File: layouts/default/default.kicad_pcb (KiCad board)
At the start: 2 copper layers, 66 parts

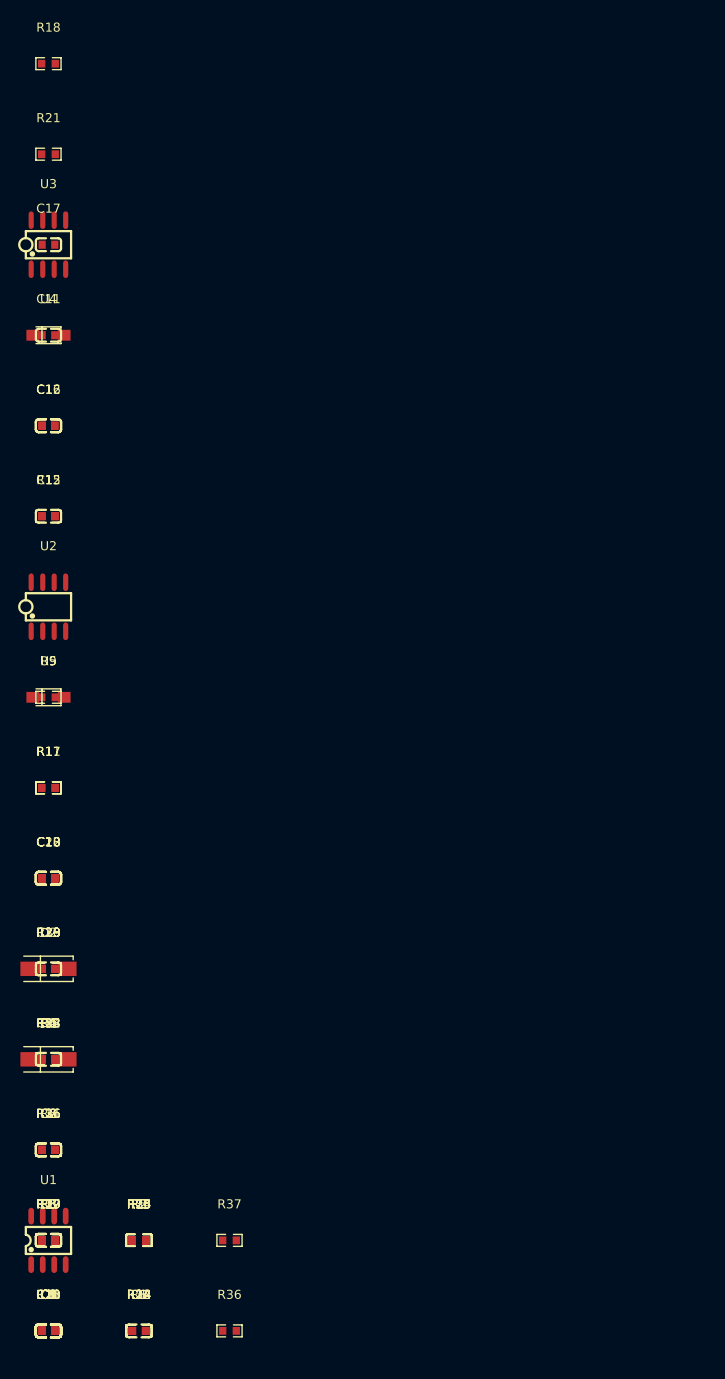
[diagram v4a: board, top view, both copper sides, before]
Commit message: Added plugin to show atopile_address on layout
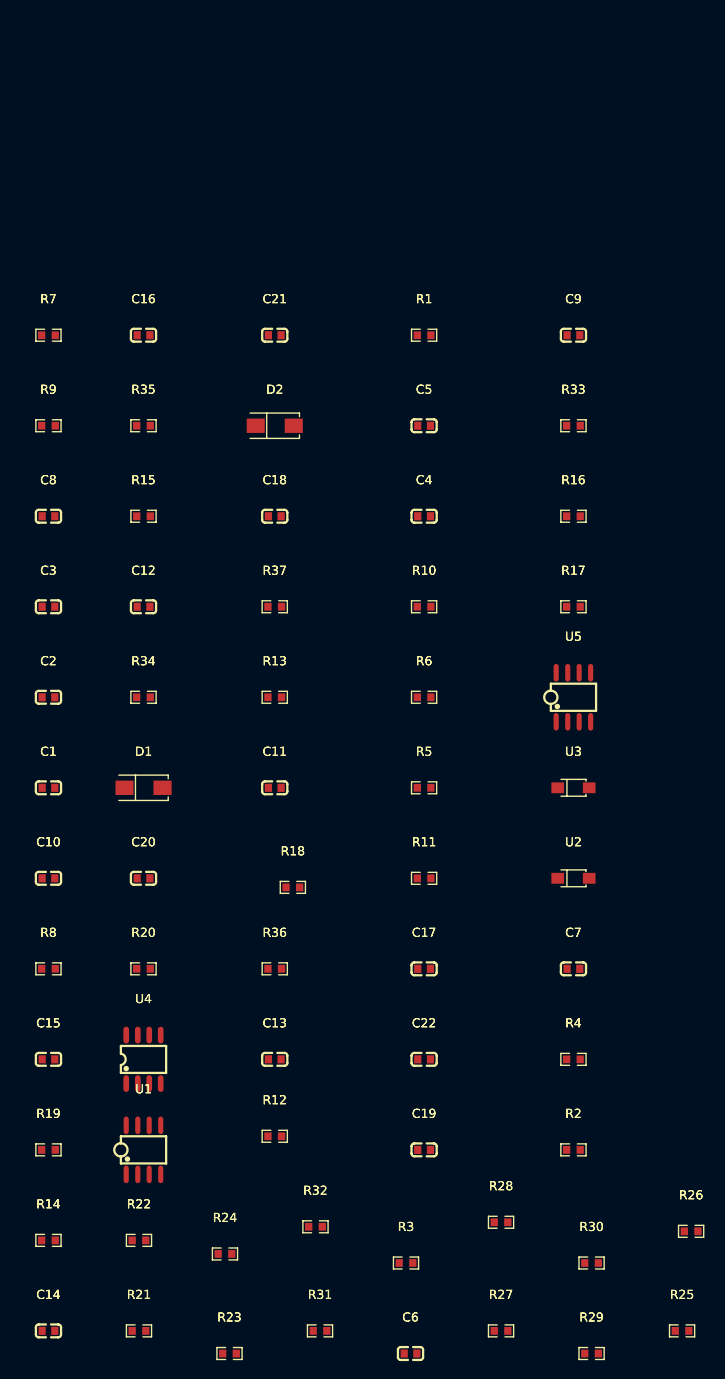
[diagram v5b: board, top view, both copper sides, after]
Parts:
- U1: footprint atopile:SOP-8_L4.9-W3.9-P1.27-LS6.0-BL-0d1ac6 -> atopile:SOIC-8_L5.0-W4.0-P1.27-LS6.0-BL-294f77
- U2, U3: footprint atopile:SOIC-8_L5.0-W4.0-P1.27-LS6.0-BL-294f77 -> atopile:SOD-123FL_L2.7-W1.8-LS3.8-RD-0c8348
- U4: footprint atopile:SOD-123FL_L2.7-W1.8-LS3.8-RD-0c8348 -> atopile:SOP-8_L4.9-W3.9-P1.27-LS6.0-BL-0d1ac6
- U5: footprint atopile:SOD-123FL_L2.7-W1.8-LS3.8-RD-0c8348 -> atopile:SOIC-8_L5.0-W4.0-P1.27-LS6.0-BL-294f77
- moved R21 130.4 mm to (10.0, 0.00)
- moved C9 124.4 mm to (58.0, -110.0)
- moved R1 114.4 mm to (41.5, -110.0)
- moved C21 112.8 mm to (25.0, -110.0)
- moved C4 99.1 mm to (41.5, -90.0)
- moved C5 99.1 mm to (41.5, -100.0)
- moved R18 94.9 mm to (27.0, -49.0)
- moved R16 90.9 mm to (58.0, -90.0)
- moved R15 90.6 mm to (10.5, -90.0)
- moved C8 90.6 mm to (0.00, -90.0)
- moved C17 90.1 mm to (41.5, -40.0)
- moved R10 90.1 mm to (41.5, -80.0)
- moved R35 90.0 mm to (10.5, -100.0)
- moved R7 90.0 mm to (0.00, -110.0)
- moved R33 83.5 mm to (58.0, -100.0)
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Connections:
- C1 pad 1: hv-1 -> net-2
- C1 pad 2: gnd-2 -> non_inverting_input
- C10 pad 1: INPUT-1 -> net-6
- C10 pad 2: resistors_ifs[0] -> P1INminus
- C11 pad 1: resistors_ifs[0] -> non_inverting_input
- C11 pad 2: net-6 -> line-1
- C12 pad 1: net-2 -> line-1
- C12 pad 2: net -> resistors_ifs[0]-2
- C13 pad 1: net-1 -> net-8
- C13 pad 2: P1INminus -> P2INminus-1
- C14 pad 1: line-1 -> P2INminus-1
- C14 pad 2: resistors_ifs[0]-1 -> P2OUT-1
- C15 pad 1: net-5 -> P2OUT-1
- C15 pad 2: P2INminus -> net
- C16 pad 1: P2INminus -> cathode
- C16 pad 2: P2OUT -> net-1
- C17 pad 1: P2OUT -> non_inverting_input
- C17 pad 2: net-7 -> gnd-2
- C18 pad 1: cathode -> P2OUT
- C18 pad 2: net -> net-7
- C19 pad 1: P1INminus -> VCCplus
- C19 pad 2: output -> gnd-2
- C2 pad 1: non_inverting_input -> hv-1
- C20 pad 1: wiper-1 -> gnd
- C20 pad 2: P2INminus-1 -> gnd-2
- C21 pad 1: non_inverting_input -> P1INminus
- C21 pad 2: net-4 -> output
- C22 pad 1: P2OUT-1 -> wiper
- C22 pad 2: net-8 -> P2INminus
- C3 pad 1: gnd -> CAPminus
- C3 pad 2: gnd-2 -> CAPplus
- C4 pad 1: CAPminus -> CAPplus
- C4 pad 2: CAPplus -> anode
- C5 pad 1: CAPplus -> non_inverting_input
- C5 pad 2: cathode-1 -> net-5
- C6 pad 1: VCCplus -> line
- C6 pad 2: gnd-2 -> ff1_low_pass-gnd
- C7 pad 1: net-3 -> INPUT
- C7 pad 2: non_inverting_input -> resistors_ifs[0]-3
- C8 pad 1: line -> resistors_ifs[0]-3
- C8 pad 2: ff1_low_pass-gnd -> net-4
- C9 pad 1: non_inverting_input -> net-3
- C9 pad 2: line-1 -> net-1
- D1 pad 1: cathode-1 -> anode
- D2 pad 2: cathode-1 -> anode
- R1 pad 1: non_inverting_input -> net-5
- R10 pad 1: wiper -> wiper-1
- R10 pad 2: net-2 -> net-6
- R11 pad 1: wiper -> line-1
- R11 pad 2: P1INminus -> resistors_ifs[0]-2
- R12 pad 1: wiper -> resistors_ifs[1]
- R12 pad 2: net-1 -> net-8
- R13 pad 1: resistors_ifs[0] -> net-8
- R13 pad 2: wiper -> P2INminus-1
- R14 pad 1: non_inverting_input -> P2INminus-1
- R14 pad 2: wiper -> P2OUT-1
- R15 pad 1: P1INminus -> net
- R15 pad 2: output -> cathode
- R16 pad 1: line-1 -> net-1
- R16 pad 2: resistors_ifs[0]-1 -> P1INminus
- R17 pad 1: resistors_ifs[1]-1 -> input_dc_bias_r-net
- R17 pad 2: net-5 -> input_dc_bias_r-net-1
- R18 pad 1: net-5 -> INPUT
- R18 pad 2: P2INminus -> net-2
- R19 pad 1: P2INminus -> net-7
- R19 pad 2: P2OUT -> resistors_ifs[0]
- R2 pad 1: hv-1 -> net-5
- R2 pad 2: non_inverting_input -> hv
- R20 pad 1: net-7 -> INPUT-1
- R20 pad 2: cathode -> gnd-2
- R21 pad 1: net -> INPUT-1
- R21 pad 2: P1INminus -> gnd-1
- R22 pad 1: resistors_ifs[0]-1 -> hv
- R22 pad 2: non_inverting_input -> INPUT-1
- R23 pad 1: resistors_ifs[1]-1 -> non_inverting_input
- R23 pad 2: non_inverting_input -> gnd-2
- R24 pad 1: resistors_ifs[0]-2 -> hv-1
- R24 pad 2: wiper-1 -> non_inverting_input
- R25 pad 1: resistors_ifs[1] -> resistors_ifs[0]-2
- R25 pad 2: wiper-1 -> non_inverting_input
- R26 pad 1: output -> resistors_ifs[1]
- R26 pad 2: resistors_ifs[1] -> non_inverting_input
- R27 pad 1: output -> resistors_ifs[0]-3
- R27 pad 2: P2INminus-1 -> wiper-1
- R28 pad 1: resistors_ifs[0]-2 -> non_inverting_input
- R28 pad 2: P2OUT-1 -> wiper-1
- R29 pad 1: P2INminus-1 -> resistors_ifs[0]
- R29 pad 2: P2OUT-1 -> gnd-1
- R3 pad 1: input_dc_bias_r-net -> line-1
- R3 pad 2: input_dc_bias_r-net-1 -> line
- R30 pad 1: net-4 -> gnd-2
- R30 pad 2: gnd-2 -> gnd-1
- R31 pad 1: net-4 -> resistors_ifs[0]-1
- R31 pad 2: hv -> wiper
- R32 pad 1: net-8 -> resistors_ifs[1]-1
- R32 pad 2: resistors_ifs[0]-3 -> wiper
- R33 pad 1: INPUT -> P1INminus
- R33 pad 2: gnd-2 -> output
- R34 pad 1: INPUT -> output
- R34 pad 2: gnd-1 -> resistors_ifs[1]-1
- R35 pad 1: hv -> output
- R35 pad 2: INPUT -> P2INminus
- R36 pad 1: resistors_ifs[0]-3 -> resistors_ifs[0]-1
- R36 pad 2: gnd-1 -> P2OUT
- R37 pad 1: gnd-2 -> P2INminus
- R37 pad 2: gnd-1 -> P2OUT
- R4 pad 1: INPUT-1 -> line
- R4 pad 2: net-3 -> P1INminus
- R5 pad 1: line-1 -> INPUT
- R5 pad 2: line -> resistors_ifs[0]-3
- R6 pad 1: line -> resistors_ifs[0]-3
- R6 pad 2: P1INminus -> non_inverting_input
- R7 pad 1: INPUT-1 -> net-4
- R7 pad 2: resistors_ifs[0] -> non_inverting_input
- R8 pad 1: resistors_ifs[0] -> wiper-1
- R8 pad 2: non_inverting_input -> net-3
- R9 pad 1: net-6 -> wiper-1
- R9 pad 2: non_inverting_input -> P1INminus
- U1 pad 1: hv-1 -> non_inverting_input
- U1 pad 2: CAPplus -> gain_opamps-P1INminus
- U1 pad 3: gnd-2 -> non_inverting_input
- U1 pad 4: CAPminus -> gnd-2
- U1 pad 5: gnd -> resistors_ifs[0]-2
- U1 pad 6: LV -> P2INminus-1
- U1 pad 7: OSC -> P2OUT-1
- U2 pad 1: non_inverting_input -> gnd-2
- U2 pad 2: gain_opamps-P1INminus -> cathode
- U3 pad 1: output -> cathode
- U3 pad 2: P1INminus -> gnd-2
- U4 pad 1: gnd-2 -> hv-1
- U4 pad 2: cathode -> CAPplus
- U5 pad 1: cathode -> output
- U5 pad 2: gnd-2 -> P1INminus

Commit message: rearranged, not building. Plugin fixed
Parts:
- removed C19, C20, C21, C22: 100nF ±10% 50V X7R, atopile:C0603-bd72f6
- removed R23, R24, R25, R26, R27, R28, R29, R30, R31, R32, R33, R34, R35, R36, R37: 10kΩ ±1% 100mW, atopile:R0603-ebcab9
- added D3: , atopile:SMA_L4.3-W2.5-LS5.0-RD-e683d9, F.Cu at (40.0, -90.0)
- C10, C11, C14, C15, C17, C18: value 100nF ±10% 50V X7R -> 1µF ±10% 25V X5R; footprint atopile:C0603-bd72f6 -> atopile:C0402-b3ef17
- C12: value 100nF ±10% 50V X7R -> 100nF ±10% 16V X7R; footprint atopile:C0603-bd72f6 -> atopile:C0402-b3ef17
- C13, C16: value 100nF ±10% 50V X7R -> 47µF ±20% 25V X5R; footprint atopile:C0603-bd72f6 -> atopile:C1206-f0a137
- C2, C7: value 100nF ±10% 50V X7R -> 68nF ±10% 16V X5R; footprint atopile:C0603-bd72f6 -> atopile:C0201-a4ec75
- C3: value 100nF ±10% 50V X7R -> 390nF ±10% 16V X5R; footprint atopile:C0603-bd72f6 -> atopile:C0402-b3ef17
- C4: value 100nF ±10% 50V X7R -> 2.2nF ±10% 25V X7R; footprint atopile:C0603-bd72f6 -> atopile:C0201-a4ec75
- C5: value 100nF ±10% 50V X7R -> 27nF ±10% 25V X7R; footprint atopile:C0603-bd72f6 -> atopile:C0402-b3ef17
- C6: value 100nF ±10% 50V X7R -> 100nF ±10% 25V X7R; footprint atopile:C0603-bd72f6 -> atopile:C0402-b3ef17
- C8: value 100nF ±10% 50V X7R -> 82nF ±10% 16V X7R; footprint atopile:C0603-bd72f6 -> atopile:C0402-b3ef17
- C9: value 100nF ±10% 50V X7R -> 390pF ±5% 25V C0G; footprint atopile:C0603-bd72f6 -> atopile:C0201-a4ec75
- D1: footprint atopile:SMA_L4.3-W2.5-LS5.0-RD-e683d9 -> atopile:SOD-123_L2.7-W1.6-LS3.7-RD-30fb4b
- R1, R13, R15, R16, R17, R18, R21, R22, R5: value 10kΩ ±1% 100mW -> 1kΩ ±1% 100mW
- R10: value 10kΩ ±1% 100mW -> 2kΩ ±1% 62.5mW; footprint atopile:R0603-ebcab9 -> atopile:R0402-56259e
- R11, R2: value 10kΩ ±1% 100mW -> 15kΩ ±1% 62.5mW; footprint atopile:R0603-ebcab9 -> atopile:R0402-56259e
- R12: value 10kΩ ±1% 100mW -> 422kΩ ±1% 100mW
- R14: value 10kΩ ±1% 100mW -> 47kΩ ±1% 62.5mW; footprint atopile:R0603-ebcab9 -> atopile:R0402-56259e
- R19: value 10kΩ ±1% 100mW -> 1MΩ ±1% 100mW
- R20: value 10kΩ ±1% 100mW -> 10kΩ ±1% 62.5mW; footprint atopile:R0603-ebcab9 -> atopile:R0402-56259e
- R3: value 10kΩ ±1% 100mW -> 5.1kΩ ±1% 100mW
- R4: value 10kΩ ±1% 100mW -> 1.5kΩ ±1% 62.5mW; footprint atopile:R0603-ebcab9 -> atopile:R0402-56259e
- R6: value 10kΩ ±1% 100mW -> 22kΩ ±1% 100mW
- R7: value 10kΩ ±1% 100mW -> 27kΩ ±1% 62.5mW; footprint atopile:R0603-ebcab9 -> atopile:R0402-56259e
- R8: value 10kΩ ±1% 100mW -> 12kΩ ±1% 62.5mW; footprint atopile:R0603-ebcab9 -> atopile:R0402-56259e
- U4: footprint atopile:SOP-8_L4.9-W3.9-P1.27-LS6.0-BL-0d1ac6 -> atopile:SOIC-8_L5.0-W4.0-P1.27-LS6.0-BL-294f77
- U5: footprint atopile:SOIC-8_L5.0-W4.0-P1.27-LS6.0-BL-294f77 -> atopile:SOP-8_L4.9-W3.9-P1.27-LS6.0-BL-0d1ac6
- moved R14 220.0 mm to (0.00, -230.0)
- moved R12 219.9 mm to (0.00, -240.0)
- moved R11 175.0 mm to (0.00, -220.0)
- moved R2 160.8 mm to (0.00, -170.0)
- moved C10 160.0 mm to (0.00, -210.0)
- moved R3 157.5 mm to (0.00, -160.0)
- moved R9 150.0 mm to (0.00, -250.0)
- moved C11 132.4 mm to (0.00, -190.0)
- moved R6 117.6 mm to (0.00, -180.0)
- moved C7 115.6 mm to (0.00, -140.0)
- moved U1 110.5 mm to (0.00, -130.0)
- moved C9 107.1 mm to (0.00, -200.0)
- moved R1 102.3 mm to (20.0, -10.0)
- moved C12 94.1 mm to (60.0, 0.00)
- moved R16 93.3 mm to (10.0, -10.0)
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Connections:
- C1 pad 1: net-2 -> gain_stage-line
- C1 pad 2: non_inverting_input -> gain_stage.ff1_low_pass-gnd
- C10 pad 1: net-6 -> output
- C10 pad 2: P1INminus -> gain_stage-net-4
- C11 pad 1: non_inverting_input -> gain_stage-anode
- C11 pad 2: line-1 -> tap
- C12 pad 1: line-1 -> input_stage-net
- C12 pad 2: resistors_ifs[0]-2 -> input_stage-P1INplus
- C13 pad 1: net-8 -> hv
- C13 pad 2: P2INminus-1 -> gnd
- C14 pad 1: P2INminus-1 -> CAPminus
- C14 pad 2: P2OUT-1 -> CAPplus
- C15 pad 1: P2OUT-1 -> CAPplus
- C15 pad 2: net -> power_supply-anode
- C16 pad 1: cathode -> hv-1
- C16 pad 2: net-1 -> gnd
- C17 pad 1: non_inverting_input -> cathode
- C17 pad 2: gnd-2 -> gnd
- C18 pad 1: P2OUT -> VOUT
- C18 pad 2: net-7 -> gnd
- C2 pad 1: hv-1 -> gain_stage-line-1
- C2 pad 2: gnd-2 -> resistors_ifs[0]
- C3 pad 1: CAPminus -> resistors_ifs[0]
- C3 pad 2: CAPplus -> gain_stage-net-1
- C4 pad 1: CAPplus -> gain_stage-net-2
- C4 pad 2: anode -> tap
- C5 pad 1: non_inverting_input -> gain_stage-net-3
- C5 pad 2: net-5 -> gain_stage-line-3
- C6 pad 1: line -> output
- C6 pad 2: ff1_low_pass-gnd -> gain_stage-line-2
- C7 pad 1: INPUT -> gain_stage-line-2
- C7 pad 2: resistors_ifs[0]-3 -> gain_stage-P1INplus
- C8 pad 1: resistors_ifs[0]-3 -> gain_stage-net
- C8 pad 2: net-4 -> gain_stage-P1INminus
- C9 pad 1: net-3 -> gain_stage-P1INminus
- C9 pad 2: net-1 -> output
- D1 pad 1: anode -> hv
- D1 pad 2: hv-1 -> gnd
- D2 pad 1: VCCplus -> power_supply-anode
- D2 pad 2: anode -> hv
- R1 pad 1: net-5 -> gain_stage-line-2
- R1 pad 2: gnd-2 -> gain_stage-line
- R10 pad 1: wiper-1 -> resistors_ifs[1]
- R10 pad 2: net-6 -> gain_stage-net
- R11 pad 1: line-1 -> gain_stage-net
- R11 pad 2: resistors_ifs[0]-2 -> gain_stage-P1INminus
- R12 pad 1: resistors_ifs[1] -> gain_stage-P1INminus
- R12 pad 2: net-8 -> output
- R13 pad 1: net-8 -> gain_stage-net-4
- R13 pad 2: P2INminus-1 -> gain_stage-anode
- R14 pad 1: P2INminus-1 -> tap
- R14 pad 2: P2OUT-1 -> gain_stage-line-3
- R15 pad 1: net -> gain_stage-P1INplus
- R15 pad 2: cathode -> hv-1
- R16 pad 1: net-1 -> resistors_ifs[1]
- R16 pad 2: P1INminus -> hv-1
- R17 pad 1: input_dc_bias_r-net -> resistors_ifs[0]
- R17 pad 2: input_dc_bias_r-net-1 -> wiper
- R18 pad 1: INPUT -> hv-1
- R18 pad 2: net-2 -> wiper
- R19 pad 1: net-7 -> input_stage-P1INplus
- R19 pad 2: resistors_ifs[0] -> hv-1
- R2 pad 1: net-5 -> gain_stage-line
- R2 pad 2: hv -> gain_stage-line-3
- R20 pad 1: INPUT-1 -> input_stage-line
- R20 pad 2: gnd-2 -> input_stage-net
- R21 pad 1: INPUT-1 -> hv-1
- R21 pad 2: gnd-1 -> gnd
- R22 pad 2: INPUT-1 -> hv-1
- R3 pad 1: line-1 -> gain_stage-line-1
- R3 pad 2: line -> resistors_ifs[0]
- R4 pad 1: line -> resistors_ifs[0]
- R4 pad 2: P1INminus -> hv-1
- R5 pad 1: INPUT -> gain_stage-net-1
- R5 pad 2: resistors_ifs[0]-3 -> hv-1
- R6 pad 1: resistors_ifs[0]-3 -> wiper
- R6 pad 2: non_inverting_input -> gain_stage-net-2
- R7 pad 1: net-4 -> wiper
- R7 pad 2: non_inverting_input -> gain_stage-line-3
- R8 pad 1: wiper-1 -> wiper
- R8 pad 2: net-3 -> gain_stage-net-3
- R9 pad 1: wiper-1 -> gain_stage-line-2
- R9 pad 2: P1INminus -> gain_stage-P1INplus
- U1 pad 1: non_inverting_input -> output
- U1 pad 2: gain_opamps-P1INminus -> gain_stage-P1INminus
- U1 pad 3: non_inverting_input -> gain_stage-P1INplus
- U1 pad 4: gnd-2 -> gnd
- U1 pad 5: resistors_ifs[0]-2 -> gain_stage.gain_stage_opamp-P2INplus
- U1 pad 6: P2INminus-1 -> gain_stage.gain_stage_opamp-P2INminus
- U1 pad 7: P2OUT-1 -> gain_stage.gain_stage_opamp-P2OUT
- U1 pad 8: hv-1 -> hv
- U2 pad 1: gnd-2 -> gnd
- U2 pad 2: cathode -> gain_stage-anode
- U3 pad 1: cathode -> gain_stage-anode
- U3 pad 2: gnd-2 -> gnd
- U4 pad 1: hv-1 -> input_stage.input_buffer_opamp-P1INminus
- U4 pad 2: CAPplus -> input_stage.input_buffer_opamp-P1INminus
- U4 pad 3: gnd-2 -> input_stage-P1INplus
- U4 pad 4: CAPminus -> gnd
- U4 pad 5: gnd -> input_stage.input_buffer_opamp-P2INplus
- U4 pad 6: LV -> input_stage.input_buffer_opamp-P2INminus
- U4 pad 7: OSC -> input_stage.input_buffer_opamp-P2OUT
- U4 pad 8: hv-1 -> hv
- U5 pad 1: output -> hv
- U5 pad 2: P1INminus -> CAPplus
- U5 pad 3: non_inverting_input -> gnd
- U5 pad 4: gnd -> CAPminus
- U5 pad 5: non_inverting_input -> VOUT
- U5 pad 6: P2INminus -> LV
- U5 pad 7: P2OUT -> OSC
- U5 pad 8: VCCplus -> hv

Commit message: building
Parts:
- added C19: 4.7µF ±10% 16V X5R, atopile:C0603-bd72f6, F.Cu at (0.00, 0.00)
- added C20: 4.7µF ±10% 50V X5R, atopile:C0805-3b2e55, F.Cu at (10.0, 0.00)
- added C21: 100nF ±10% 50V X7R, atopile:C0603-bd72f6, F.Cu at (40.0, 0.00)
- added C22: 3.9nF ±10% 50V X7R, atopile:C0402-b3ef17, F.Cu at (50.0, -30.0)
- added R23: 100kΩ ±1% 62.5mW, atopile:R0402-56259e, F.Cu at (0.00, -10.0)
- added R24: 560Ω ±1% 100mW, atopile:R0603-ebcab9, F.Cu at (0.00, -20.0)
- added R25: 560Ω ±1% 100mW, atopile:R0603-ebcab9, F.Cu at (10.0, -20.0)
- added R26: 100kΩ ±1% 62.5mW, atopile:R0402-56259e, F.Cu at (10.0, -10.0)
- added R27: 1kΩ ±1% 100mW, atopile:R0603-ebcab9, F.Cu at (20.0, 0.00)
- added R28: 1kΩ ±1% 100mW, atopile:R0603-ebcab9, F.Cu at (20.0, -10.0)
- added R29: 1kΩ ±1% 100mW, atopile:R0603-ebcab9, F.Cu at (30.0, 0.00)
- added R30: 1kΩ ±1% 100mW, atopile:R0603-ebcab9, F.Cu at (30.0, -10.0)
- added R31: 1kΩ ±1% 100mW, atopile:R0603-ebcab9, F.Cu at (40.0, -20.0)
- added R32: 1kΩ ±1% 100mW, atopile:R0603-ebcab9, F.Cu at (60.0, 0.00)
- added R33: 1kΩ ±1% 100mW, atopile:R0603-ebcab9, F.Cu at (60.0, -10.0)
- added R34: 1.8kΩ ±1% 62.5mW, atopile:R0402-56259e, F.Cu at (50.0, -20.0)
- added R35: 100kΩ ±1% 62.5mW, atopile:R0402-56259e, F.Cu at (50.0, -10.0)
- added R36: 4.7kΩ ±1% 100mW, atopile:R0603-ebcab9, F.Cu at (50.0, -40.0)
- added R37: 100kΩ ±1% 62.5mW, atopile:R0402-56259e, F.Cu at (50.0, -50.0)
- added U6: , atopile:SOIC-8_L5.0-W4.0-P1.27-LS6.0-BL-294f77, F.Cu at (40.0, -10.0)
- added U7: , atopile:SOIC-8_L5.0-W4.0-P1.27-LS6.0-BL-294f77, F.Cu at (50.0, 0.00)
- C14, C15, C17, C18: value 1µF ±10% 25V X5R -> 1µF ±10% 50V X5R; footprint atopile:C0402-b3ef17 -> atopile:C0603-bd72f6
- C5: value 27nF ±10% 25V X7R -> 27nF ±10% 16V X7R
- C6: value 100nF ±10% 25V X7R -> 100nF ±10% 50V X7R; footprint atopile:C0402-b3ef17 -> atopile:C0603-bd72f6
- R10: value 2kΩ ±1% 62.5mW -> 2kΩ ±1% 100mW; footprint atopile:R0402-56259e -> atopile:R0603-ebcab9
- R12: value 422kΩ ±1% 100mW -> 422kΩ ±1% 62.5mW; footprint atopile:R0603-ebcab9 -> atopile:R0402-56259e
- R7: value 27kΩ ±1% 62.5mW -> 27kΩ ±1% 100mW; footprint atopile:R0402-56259e -> atopile:R0603-ebcab9
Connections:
- net VOUT renamed gnd-2
- net gain_stage-anode renamed gain_stage-tap-1
- net gain_stage-line-3 renamed line-1
- net gnd renamed gnd-1
- net input_stage-line renamed INPUT-1
- net output renamed gain_stage-output
- net power_supply-anode renamed anode
- net resistors_ifs[0] renamed gain_stage-resistors_ifs[0]
- net resistors_ifs[1] renamed gain_stage-resistors_ifs[1]
- net tap renamed gain_stage-tap
- net wiper renamed gain_stage-wiper
- C10 pad 2: gain_stage-net-4 -> gain_stage-net-2
- C16 pad 1: hv-1 -> hv-2
- C17 pad 1: cathode -> hv-1
- C2 pad 1: gain_stage-line-1 -> line-3
- C4 pad 1: gain_stage-net-2 -> gain_stage-net-3
- C5 pad 1: gain_stage-net-3 -> gain_stage-net
- C6 pad 2: gain_stage-line-2 -> gain_stage-line-1
- C7 pad 1: gain_stage-line-2 -> gain_stage-line-1
- C8 pad 1: gain_stage-net -> gain_stage-net-4
- D3 pad 1: cathode -> hv-1
- R1 pad 1: gain_stage-line-2 -> gain_stage-line-1
- R10 pad 2: gain_stage-net -> gain_stage-net-4
- R11 pad 1: gain_stage-net -> gain_stage-net-4
- R13 pad 1: gain_stage-net-4 -> gain_stage-net-2
- R15 pad 2: hv-1 -> hv-2
- R16 pad 2: hv-1 -> hv-2
- R18 pad 1: hv-1 -> hv-2
- R19 pad 2: hv-1 -> hv-2
- R21 pad 1: hv-1 -> hv-2
- R22 pad 2: hv-1 -> hv-2
- R3 pad 1: gain_stage-line-1 -> line-3
- R4 pad 2: hv-1 -> hv-2
- R5 pad 2: hv-1 -> hv-2
- R6 pad 2: gain_stage-net-2 -> gain_stage-net-3
- R8 pad 2: gain_stage-net-3 -> gain_stage-net
- R9 pad 1: gain_stage-line-2 -> gain_stage-line-1
